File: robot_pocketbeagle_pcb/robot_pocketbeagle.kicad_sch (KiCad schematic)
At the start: 76 parts, among them J1 QMC5883L, J10 driver_dvr8833, J11 12V_DC, J12 IN_DVR8833, J13 9V_DC_DC, J14 servo_x_y, J15 shr05, J16 5V_DC_DC, J17 Conn_GND, J18 Conn_5V, J19 Conn_pwm_out_b, J2 USB_A, J20 Conn_pwm_out_a, J21 Conn_P2_3.3V, J26 Conn_12.6V, J29 Conn_AIN_4.096_3.3_1.8V, J3 UART0, J30 Conn_5V, J31 Conn_GPI028_34, J4 P1, J5 MPU6050, J6 ADS1115, J7 P2, J8 Conn_i2c2, J9 OUT_DVR8833, Q1 BC847, Q2 D90N02L, Q3 D90N02L, U1 PC817, U2 PC817, U3 74HC00, U4 LM358

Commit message: update pcb
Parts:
- removed J11: 12V_DC, TerminalBlock:TerminalBlock_bornier-2_P5.08mm, symbol Connector:Screw_Terminal_01x02
- removed J26: Conn_12.6V, Connector_PinSocket_2.54mm:PinSocket_1x02_P2.54mm_Vertical, symbol Connector:Conn_01x02_Male
- removed Q2, Q3: D90N02L, Package_TO_SOT_SMD:TO-252-2, symbol Transistor_FET:QM6006D
- added C3, C4: 100n, Capacitor_SMD:C_0805_2012Metric, symbol Device:C
- added C5: 33n, Capacitor_SMD:C_0805_2012Metric, symbol Device:C
- added C6: 1n, Capacitor_SMD:C_0805_2012Metric, symbol Device:C
- added D1: LED, LED_THT:LED_D3.0mm, symbol Device:LED
- added Q2, Q4, Q5: BC847, Package_TO_SOT_SMD:SOT-23, symbol Transistor_BJT:BC847
- added Q3, Q6, Q7: QM6015D, Package_TO_SOT_SMD:TO-252-2, symbol Transistor_FET:QM6015D
- added R38, R39: 27, Resistor_SMD:R_0805_2012Metric, symbol Device:R
- added R40, R52, R53, R54: 0, Resistor_SMD:R_1206_3216Metric, symbol Device:R
- added R41: 2K, Resistor_SMD:R_0805_2012Metric, symbol Device:R
- added R42, R44, R45: 1K, Resistor_SMD:R_0805_2012Metric, symbol Device:R
- added R43, R46, R47: 100K, Resistor_SMD:R_0805_2012Metric, symbol Device:R
- added R48, R49, R51: 0, Resistor_SMD:R_0805_2012Metric, symbol Device:R
- added unit 3 of U3
- added unit 2 of U3
- added U5: L7805_REZERV, Package_TO_SOT_SMD:TO-252-2, symbol Regulator_Linear:L7805
- R18, R30: value 47K -> 110K
- R21: value 0,1 -> 100K; footprint Resistor_SMD:R_1206_3216Metric -> Resistor_SMD:R_0805_2012Metric
- R31: value 250 -> 100K
- R33, R34, R35, R36, R37: value 0,1 -> 0
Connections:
- net 12.6V_BAT_IN: now also C2.1, J13.2 (Pin_2), U4.8 (V+), C5.1, U5.1 (IN); no longer J13.1 (Pin_1), R21.1
- net GND_SYS: no longer C1.2, C2.2, J1.2 (Pin_2), J12.8 (Pin_8), J14.3 (Pin_3), J14.6 (Pin_6), J15.4 (Pin_4), J16.1 (Pin_1), J17.1 (Pin_1), J17.2 (Pin_2), J17.3 (Pin_3), J17.4 (Pin_4), J17.5 (Pin_5), J17.6 (Pin_6), J17.7 (Pin_7), J17.8 (Pin_8), J17.9 (Pin_9), J2.4 (GND), J2.5 (Shield), J3.1 (Pin_1), J4.13 (Pin_13), J4.15 (Pin_15), J4.16 (Pin_16), J4.22 (Pin_22), J5.2 (Pin_2), J6.2 (Pin_2), J7.15 (Pin_15), J7.21 (Pin_21), J8.2 (Pin_2), Q1.2 (E), R11.1, R13.1, R15.1, R17.1, R18.1, R20.2, R22.1, R30.2, R33.1, R33.2, R34.1, R34.2, R35.1, R35.2, R9.1, U1.2, U1.3, U2.2, U2.3, U3.7 (GND), U4.4 (V-)
- net P1_SCL_I2C2: now also R39.1
- net P1_SDA_I2C2: now also R38.1
- net P1_SYS_VIN: now also Q3.3 (S), Q6.3 (S), R38.2, R39.2; no longer C1.1, C2.1, J18.1 (Pin_1), R31.1, U3.14 (VCC), U4.8 (V+)
- net P2_GPIO9_OUT_mosfet: now also U3.10; no longer U3.12
- net at U3.3: now also R42.2, U3.4, U3.5; no longer R18.2
- net GND: now reaches R21.2
- net GND: now also C1.2, C2.2, H1.1, H2.1, H3.1, H4.1, J1.2 (Pin_2), J12.8 (Pin_8), J14.3 (Pin_3), J14.6 (Pin_6), J15.4 (Pin_4), J16.1 (Pin_1), J17.1 (Pin_1), J17.2 (Pin_2), J17.3 (Pin_3), J17.4 (Pin_4), J17.5 (Pin_5), J17.6 (Pin_6), J17.7 (Pin_7), J17.8 (Pin_8), J17.9 (Pin_9), J2.4 (GND), J2.5 (Shield), J3.1 (Pin_1), J4.16 (Pin_16), J4.22 (Pin_22), J5.2 (Pin_2), J6.2 (Pin_2), J7.15 (Pin_15), J7.21 (Pin_21), J8.2 (Pin_2), J9.8 (Pin_8), Q1.2 (E), R11.1, R13.1, R15.1, R17.1, R20.2, R22.1, R31.2, R33.1, R33.2, R34.1, R34.2, R35.1, R35.2, R9.1, U1.2, U1.3, U2.2, U2.3, U3.7 (GND), U4.4 (V-), C3.2, C4.2, C5.2, C6.2, D1.1 (K), Q2.2 (E), Q4.2 (E), Q5.2 (E), R40.1, R40.2, R48.1, R48.2, R49.1, R49.2, R51.1, R51.2, R53.1, R53.2, R54.1, R54.2, U5.2 (GND)
- net at U4.1: now also R18.1; no longer U3.1
- net at U3.11: now also R45.1; no longer R30.1
- net 5V_SYS_VIN_IN: now reaches J16.2 (Pin_2), J18.2 (Pin_2)
- net 5V_SYS_VIN_IN: now also J18.1 (Pin_1), C3.1, C4.1, Q6.2 (D), R46.1, R52.1, R52.2
- net at U4.7: now also R30.1; no longer U3.2
- net at U3.13: now also U3.12, U3.8; no longer R31.2
- net 9V_DRIVER_DC_DC renamed 9V_DRIVER_DC_DC_IN
- net 9V_DRIVER_DC_DC_IN: now also J13.1 (Pin_1), Q7.2 (D), R47.1; no longer J13.2 (Pin_2), J9.1 (Pin_1)
- net P1_DN_USB renamed P1_USB_D_N
- net P1_DP_USB renamed P1_USB_D_P
- new net: Q5.3 (C), Q7.1 (G), R47.2
- new net: R30.2, R31.1, U3.9
- new net: R44.1, U3.6
- new net: Q5.1 (B), R45.2
- new net: Q4.1 (B), R44.2
- new net: Q4.3 (C), Q6.1 (G), R46.2
- new net: Q2.3 (C), Q3.1 (G), R43.2
- new net: D1.2 (A), R41.2
- new net: R18.2, R21.1, U3.1, U3.2
- new net: Q2.1 (B), R42.1
- new net 9V_DRIVER_DC_DC_OUT: J9.1 (Pin_1), Q7.3 (S), R41.1
- new net AUX_5V_OUT: C1.1, C6.1, Q3.2 (D), R43.1, U3.14 (VCC), U5.3 (OUT)
- new net P1_ID_USB: J4.13 (Pin_13), J4.15 (Pin_15)
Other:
- moved on the sheet: BZ1, C1, C2, H1, H2, H3, H4, J1, J12, J13, J16, J17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

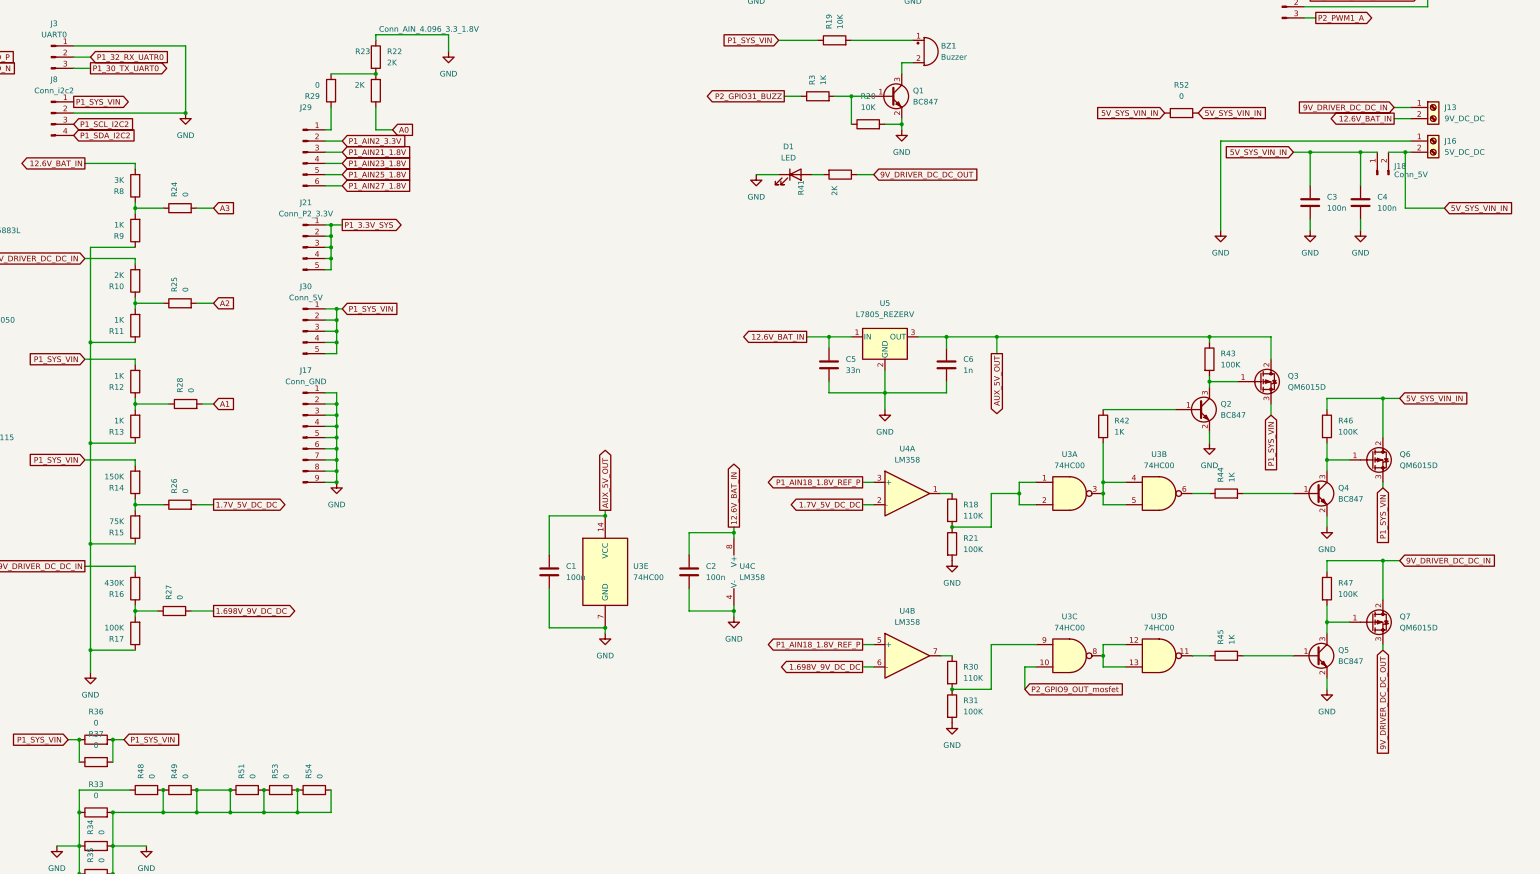
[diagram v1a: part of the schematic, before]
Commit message: add sim. shem and fix board shem
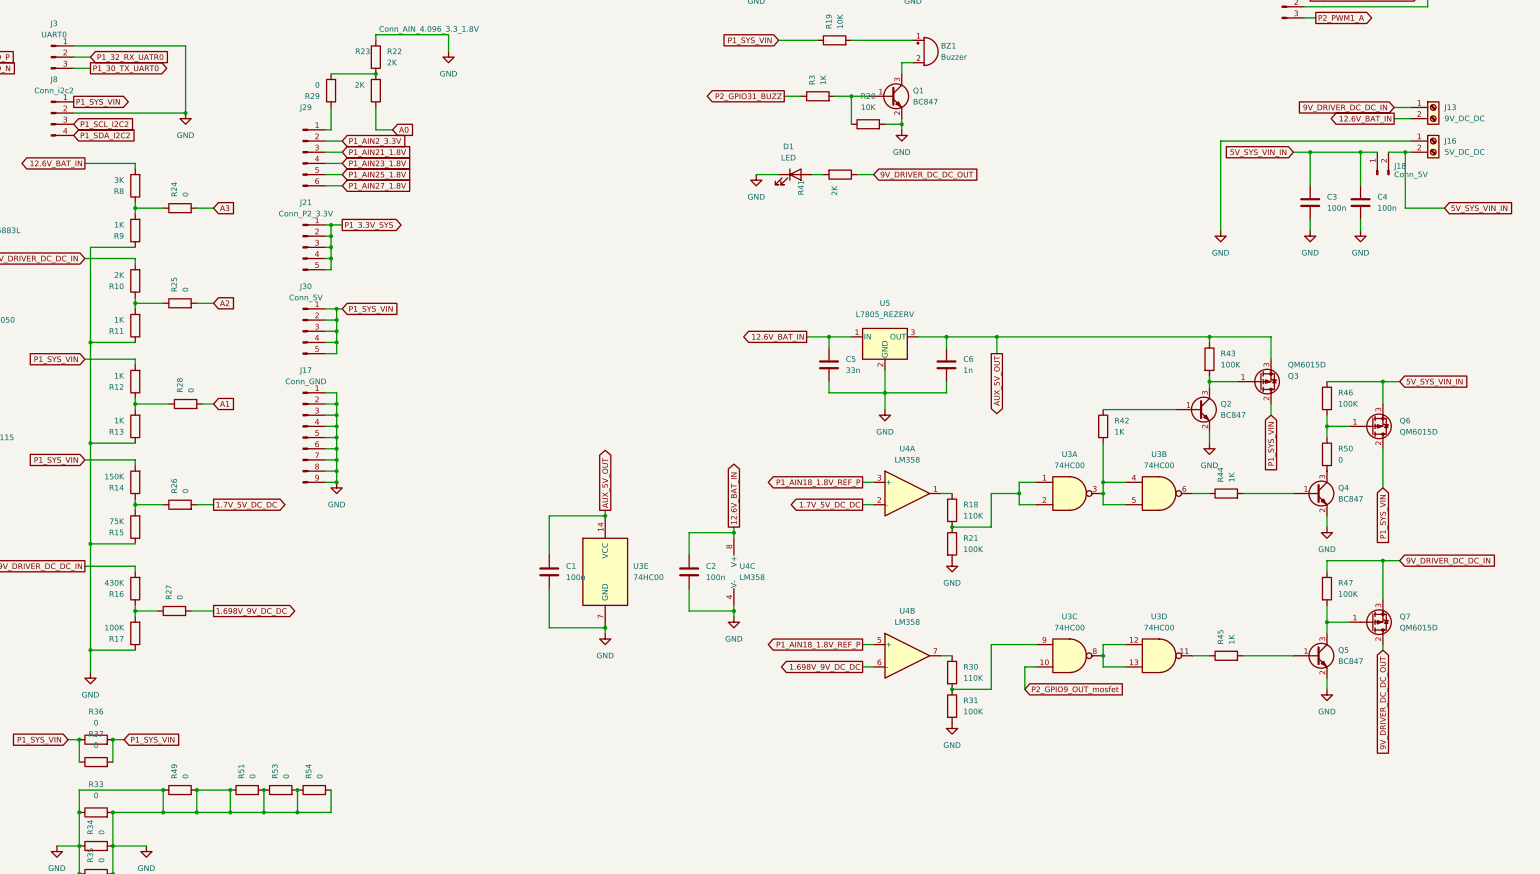
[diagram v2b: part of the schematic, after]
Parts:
- removed R48: 0, Resistor_SMD:R_0805_2012Metric, symbol Device:R
- removed R52: 0, Resistor_SMD:R_1206_3216Metric, symbol Device:R
- added R50: 0, Resistor_SMD:R_1206_3216Metric, symbol Device:R
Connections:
- net 5V_SYS_VIN_IN: now also Q6.3 (S); no longer Q6.2 (D)
- net 9V_DRIVER_DC_DC_IN: now also Q7.3 (S); no longer Q7.2 (D)
- net 9V_DRIVER_DC_DC_OUT: now also Q7.2 (D); no longer Q7.3 (S)
- net AUX_5V_OUT: now also Q3.3 (S); no longer Q3.2 (D)
- net P1_SYS_VIN: now also Q3.2 (D), Q6.2 (D); no longer Q3.3 (S), Q6.3 (S)
- net at Q6.1 (G), R46.2: now also R50.1; no longer Q4.3 (C)
- new net: Q4.3 (C), R50.2
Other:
- moved on the sheet: Q6, R46

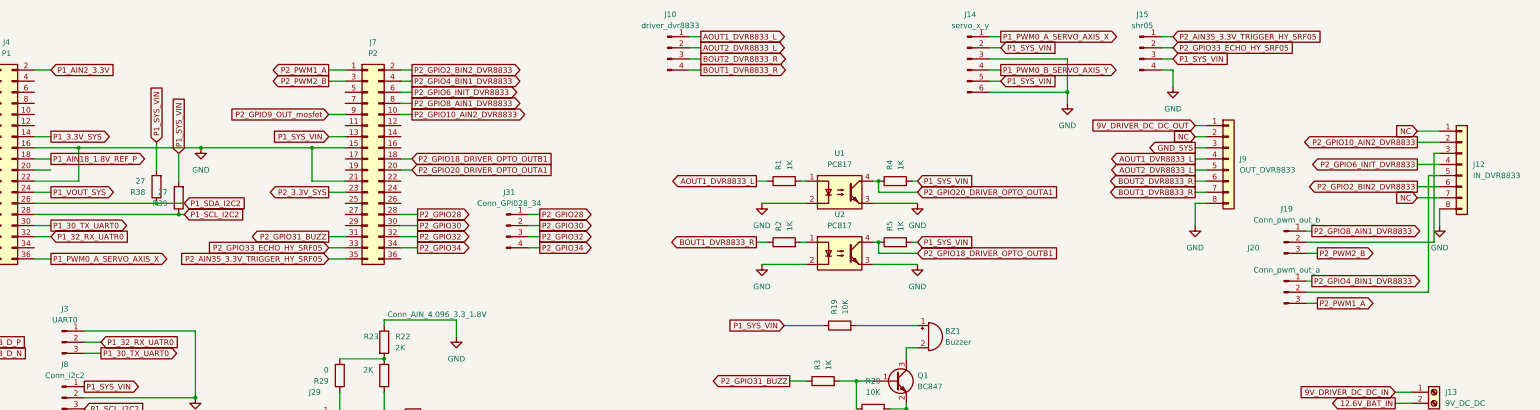
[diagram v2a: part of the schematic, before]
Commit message: fix board optopara
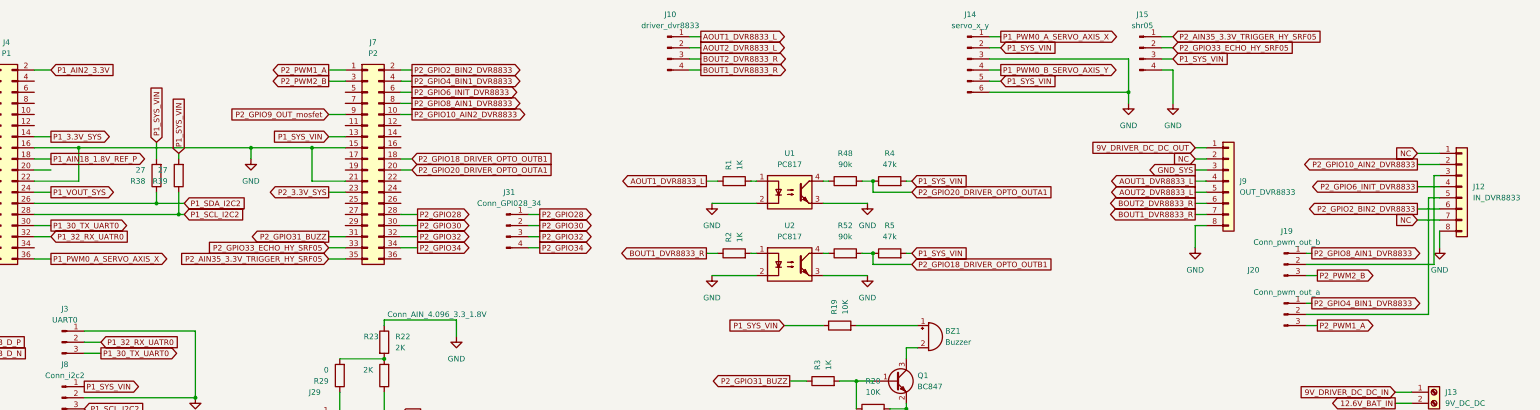
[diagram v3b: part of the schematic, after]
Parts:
- added R48, R52: 90k, Resistor_SMD:R_0805_2012Metric, symbol Device:R
- R4, R5: value 1K -> 47k
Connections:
- net P2_GPIO18_DRIVER_OPTO_OUTB1: now also R52.2; no longer U2.4
- net P2_GPIO20_DRIVER_OPTO_OUTA1: now also R48.2; no longer U1.4
- new net: R52.1, U2.4
- new net: R48.1, U1.4
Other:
- moved on the sheet: J12, J19, J20, J9, R1, R2, R38, R39, R4, R5, U1, U2

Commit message: board debugging
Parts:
- added R55, R56, R57: 1K, Resistor_SMD:R_0805_2012Metric, symbol Device:R
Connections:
- net GND: now also R55.1, R56.2, R57.2
- net at Q5.1 (B), R45.2: now also R57.1
- net at Q4.1 (B), R44.2: now also R56.1
- net at Q2.1 (B), R42.1: now also R55.2
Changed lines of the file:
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@@
   (junction (at 110.49 44.45) (diameter 0) (color 0 0 0 0)
   )
+  (junction (at 306.07 168.91) (diameter 0) (color 0 0 0 0)
+  )
   (junction (at 271.78 195.58) (diameter 0) (color 0 0 0 0)
   )
@@
   (junction (at 81.28 274.32) (diameter 0) (color 0 0 0 0)
   )
+  (junction (at 341.63 187.96) (diameter 0) (color 0 0 0 0)
+  )
   (junction (at 222.25 214.63) (diameter 0) (color 0 0 0 0)
   )
@@
   (junction (at 132.08 172.72) (diameter 0) (color 0 0 0 0)
   )
+  (junction (at 341.63 224.79) (diameter 0) (color 0 0 0 0)
+  )
   (junction (at 132.08 182.88) (diameter 0) (color 0 0 0 0)
   )
@@
     (stroke (width 0) (type default) (color 0 0 0 0))
   )
+  (wire (pts (xy 341.63 224.79) (xy 349.25 224.79))
+    (stroke (width 0) (type default) (color 0 0 0 0))
+  )
   (wire (pts (xy 227.33 115.57) (xy 232.41 115.57))
     (stroke (width 0) (type default) (color 0 0 0 0))
@@
     (stroke (width 0) (type default) (color 0 0 0 0))
   )
-  (wire (pts (xy 337.82 187.96) (xy 349.25 187.96))
+  (wire (pts (xy 337.82 187.96) (xy 341.63 187.96))
     (stroke (width 0) (type default) (color 0 0 0 0))
   )
@@
     (stroke (width 0) (type default) (color 0 0 0 0))
   )
+  (wire (pts (xy 294.64 161.29) (xy 306.07 161.29))
+    (stroke (width 0) (type default) (color 0 0 0 0))
+  )
   (wire (pts (xy 241.3 52.07) (xy 242.57 52.07))
     (stroke (width 0) (type default) (color 0 0 0 0))
@@
     (stroke (width 0) (type default) (color 0 0 0 0))
   )
+  (wire (pts (xy 294.64 168.91) (xy 294.64 161.29))
+    (stroke (width 0) (type default) (color 0 0 0 0))
+  )
   (wire (pts (xy 213.36 26.67) (xy 210.82 26.67))
     (stroke (width 0) (type default) (color 0 0 0 0))
@@
     (stroke (width 0) (type default) (color 0 0 0 0))
   )
-  (wire (pts (xy 337.82 224.79) (xy 349.25 224.79))
+  (wire (pts (xy 337.82 224.79) (xy 341.63 224.79))
     (stroke (width 0) (type default) (color 0 0 0 0))
   )
@@
     (stroke (width 0) (type default) (color 0 0 0 0))
   )
+  (wire (pts (xy 341.63 187.96) (xy 349.25 187.96))
+    (stroke (width 0) (type default) (color 0 0 0 0))
+  )
   (wire (pts (xy 60.96 52.07) (xy 71.12 52.07))
     (stroke (width 0) (type default) (color 0 0 0 0))
@@
     (stroke (width 0) (type default) (color 0 0 0 0))
   )
+  (wire (pts (xy 341.63 228.6) (xy 341.63 224.79))
+    (stroke (width 0) (type default) (color 0 0 0 0))
+  )
   (wire (pts (xy 24.13 248.92) (xy 24.13 256.54))
     (stroke (width 0) (type default) (color 0 0 0 0))
@@
     (stroke (width 0) (type default) (color 0 0 0 0))
   )
+  (wire (pts (xy 341.63 187.96) (xy 341.63 190.5))
+    (stroke (width 0) (type default) (color 0 0 0 0))
+  )
   (wire (pts (xy 379.73 55.88) (xy 382.27 55.88))
     (stroke (width 0) (type default) (color 0 0 0 0))
@@
     (stroke (width 0) (type default) (color 0 0 0 0))
   )
+  (wire (pts (xy 341.63 199.39) (xy 341.63 198.12))
+    (stroke (width 0) (type default) (color 0 0 0 0))
+  )
   (wire (pts (xy 123.19 260.35) (xy 123.19 255.27))
     (stroke (width 0) (type default) (color 0 0 0 0))
@@
     (stroke (width 0) (type default) (color 0 0 0 0))
   )
+  (wire (pts (xy 341.63 237.49) (xy 341.63 236.22))
+    (stroke (width 0) (type default) (color 0 0 0 0))
+  )
   (wire (pts (xy 306.07 176.53) (xy 306.07 185.42))
     (stroke (width 0) (type default) (color 0 0 0 0))
@@
     (pin "2")
   )
+  (symbol (lib_id "power:GND") (at 341.63 237.49 0) (unit 1)
+    (in_bom yes) (on_board yes) (fields_autoplaced)
+    (property "Reference" "#PWR0133" (id 0) (at 341.63 243.84 0)
+      (effects (font (size 1.27 1.27)) hide)
+    )
+    (property "Value" "GND" (id 1) (at 341.63 242.57 0))
+    (property "Footprint" "" (id 2) (at 341.63 237.49 0)
+      (effects (font (size 1.27 1.27)) hide)
+    )
+    (property "Datasheet" "" (id 3) (at 341.63 237.49 0)
+      (effects (font (size 1.27 1.27)) hide)
+    )
+    (pin "1")
+  )
   (symbol (lib_id "Device:R") (at 86.36 149.86 180) (unit 1)
     (in_bom yes) (on_board yes)
@@
     (pin "2")
   )
+  (symbol (lib_id "power:GND") (at 294.64 168.91 0) (unit 1)
+    (in_bom yes) (on_board yes) (fields_autoplaced)
+    (property "Reference" "#PWR0132" (id 0) (at 294.64 175.26 0)
+      (effects (font (size 1.27 1.27)) hide)
+    )
+    (property "Value" "GND" (id 1) (at 294.64 173.99 0))
+    (property "Footprint" "" (id 2) (at 294.64 168.91 0)
+      (effects (font (size 1.27 1.27)) hide)
+    )
+    (property "Datasheet" "" (id 3) (at 294.64 168.91 0)
+      (effects (font (size 1.27 1.27)) hide)
+    )
+    (pin "1")
+  )
   (symbol (lib_id "74xx:74HC00") (at 193.04 205.74 0) (unit 5)
     (in_bom yes) (on_board yes) (fields_autoplaced)
@@
     (pin "2")
   )
+  (symbol (lib_id "power:GND") (at 341.63 199.39 0) (unit 1)
+    (in_bom yes) (on_board yes) (fields_autoplaced)
+    (property "Reference" "#PWR0134" (id 0) (at 341.63 205.74 0)
+      (effects (font (size 1.27 1.27)) hide)
+    )
+    (property "Value" "GND" (id 1) (at 341.63 204.47 0))
+    (property "Footprint" "" (id 2) (at 341.63 199.39 0)
+      (effects (font (size 1.27 1.27)) hide)
+    )
+    (property "Datasheet" "" (id 3) (at 341.63 199.39 0)
+      (effects (font (size 1.27 1.27)) hide)
+    )
+    (pin "1")
+  )
   (symbol (lib_id "Connector:Conn_01x05_Male") (at 124.46 132.08 0) (unit 1)
     (in_bom yes) (on_board yes) (fields_autoplaced)
@@
     (pin "3")
   )
+  (symbol (lib_id "Device:R") (at 341.63 194.31 0) (unit 1)
+    (in_bom yes) (on_board yes)
+    (property "Reference" "R56" (id 0) (at 344.17 193.0399 0)
+      (effects (font (size 1.27 1.27)) (justify left))
+    )
+    (property "Value" "1K" (id 1) (at 344.17 195.5799 0)
+      (effects (font (size 1.27 1.27)) (justify left))
+    )
+    (property "Footprint" "Resistor_SMD:R_0805_2012Metric" (id 2) (at 339.852 194.31 90)
+      (effects (font (size 1.27 1.27)) hide)
+    )
+    (property "Datasheet" "~" (id 3) (at 341.63 194.31 0)
+      (effects (font (size 1.27 1.27)) hide)
+    )
+    (pin "1")
+    (pin "2")
+  )
   (symbol (lib_id "Device:R") (at 77.47 260.35 90) (unit 1)
     (in_bom yes) (on_board yes)
@@
     (pin "3")
   )
+  (symbol (lib_id "Device:R") (at 306.07 165.1 0) (unit 1)
+    (in_bom yes) (on_board yes)
+    (property "Reference" "R55" (id 0) (at 308.61 163.8299 0)
+      (effects (font (size 1.27 1.27)) (justify left))
+    )
+    (property "Value" "1K" (id 1) (at 308.61 166.3699 0)
+      (effects (font (size 1.27 1.27)) (justify left))
+    )
+    (property "Footprint" "Resistor_SMD:R_0805_2012Metric" (id 2) (at 304.292 165.1 90)
+      (effects (font (size 1.27 1.27)) hide)
+    )
+    (property "Datasheet" "~" (id 3) (at 306.07 165.1 0)
+      (effects (font (size 1.27 1.27)) hide)
+    )
+    (pin "1")
+    (pin "2")
+  )
   (symbol (lib_id "Connector:Conn_01x05_Male") (at 124.46 151.13 0) (unit 1)
     (in_bom yes) (on_board yes)
@@
     (pin "2")
   )
+  (symbol (lib_id "Device:R") (at 341.63 232.41 0) (unit 1)
+    (in_bom yes) (on_board yes)
+    (property "Reference" "R57" (id 0) (at 344.17 231.1399 0)
+      (effects (font (size 1.27 1.27)) (justify left))
+    )
+    (property "Value" "1K" (id 1) (at 344.17 233.6799 0)
+      (effects (font (size 1.27 1.27)) (justify left))
+    )
+    (property "Footprint" "Resistor_SMD:R_0805_2012Metric" (id 2) (at 339.852 232.41 90)
+      (effects (font (size 1.27 1.27)) hide)
+    )
+    (property "Datasheet" "~" (id 3) (at 341.63 232.41 0)
+      (effects (font (size 1.27 1.27)) hide)
+    )
+    (pin "1")
+    (pin "2")
+  )
   (symbol (lib_id "Connector:Conn_01x04_Male") (at 205.74 21.59 0) (unit 1)
     (in_bom yes) (on_board yes) (fields_autoplaced)
@@
       (reference "#PWR0131") (unit 1) (value "GND") (footprint "")
     )
+    (path "/407cd1e2-f8a2-4591-af84-e5cc5d553b74"
+      (reference "#PWR0132") (unit 1) (value "GND") (footprint "")
+    )
+    (path "/08557f8c-a1db-48f4-89f3-bb640bf980ed"
+      (reference "#PWR0133") (unit 1) (value "GND") (footprint "")
+    )
+    (path "/49bba79e-27fc-463e-a0e4-d09dbe792d02"
+      (reference "#PWR0134") (unit 1) (value "GND") (footprint "")
+    )
     (path "/090e376d-2a43-4764-8521-ba5bccc689c6"
       (reference "BZ1") (unit 1) (value "Buzzer") (footprint "Buzzer_Beeper:Buzzer_12x9.5RM7.6")
@@
       (reference "R54") (unit 1) (value "0") (footprint "Resistor_SMD:R_1206_3216Metric")
     )
+    (path "/8119151c-6c53-47f5-bc3f-99f4d288f68f"
+      (reference "R55") (unit 1) (value "1K") (footprint "Resistor_SMD:R_0805_2012Metric")
+    )
+    (path "/6b2164bd-01f2-43c5-ad92-5264359e483a"
+      (reference "R56") (unit 1) (value "1K") (footprint "Resistor_SMD:R_0805_2012Metric")
+    )
+    (path "/936c9aa8-0301-4de0-b460-bafaf6ad5fca"
+      (reference "R57") (unit 1) (value "1K") (footprint "Resistor_SMD:R_0805_2012Metric")
+    )
     (path "/9e5b6597-a0e5-443e-9d55-63b44013505b"
